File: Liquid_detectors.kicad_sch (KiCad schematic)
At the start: 1 part, among them U1 AD8021AR

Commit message: ahora modifique dos sch
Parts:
- added U2: AD8655, symbol Amplifier_Operational:AD8655
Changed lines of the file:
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@@
+		)
+	)
+	(symbol
+		(lib_id "Amplifier_Operational:AD8655")
+		(at 113.03 53.34 0)
+		(unit 1)
+		(exclude_from_sim no)
+		(in_bom yes)
+		(on_board yes)
+		(dnp no)
+		(fields_autoplaced yes)
+		(property "Reference" "U2"
+			(at 123.19 46.9198 0)
+			(effects
+				(font
+					(size 1.27 1.27)
+				)
+			)
+		)
+		(property "Value" "AD8655"
+			(at 123.19 49.4598 0)
+			(effects
+				(font
+					(size 1.27 1.27)
+				)
+			)
+		)
+		(property "Footprint" ""
+			(at 114.3 52.07 0)
+			(effects
+				(font
+					(size 1.27 1.27)
+				)
+				(hide yes)
+			)
+		)
+		(property "Datasheet" "https://www.analog.com/media/en/technical-documentation/data-sheets/ad8655_8656.pdf"
+			(at 116.84 49.53 0)
+			(effects
+				(font
+					(size 1.27 1.27)
+				)
+				(hide yes)
+			)
+		)
+		(property "Description" "Single Low Noise, Precision CMOS Amplifier"
+			(at 113.03 53.34 0)
+			(effects
+				(font
+					(size 1.27 1.27)
+				)
+				(hide yes)
+			)
+		)
+		(pin "3"
+		)
+		(pin "2"
+		)
+		(pin "7"
+		)
+		(pin "4"
+		)
+		(pin "8"
+		)
+		(pin "1"
+		)
+		(pin "5"
+		)
+		(pin "6"
+		)
+		(instances
+			(project ""
+				(path "/e23e72d0-3a4b-405e-bd06-0639cdab408e"
+					(reference "U2")
+					(unit 1)
+				)
+			)
 		)
 	)

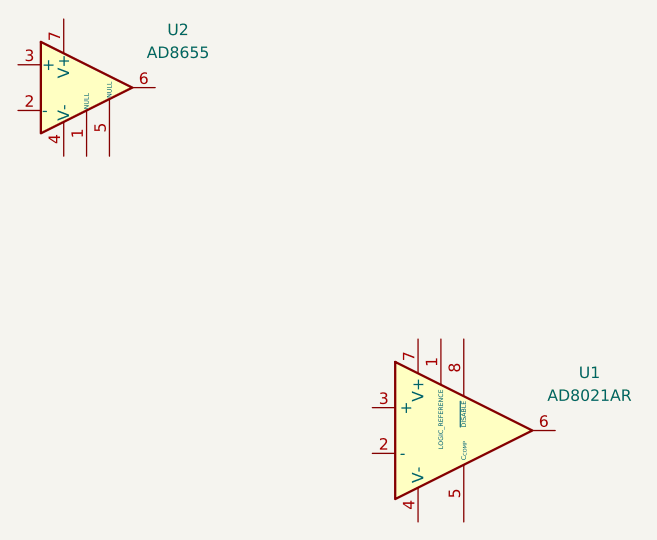
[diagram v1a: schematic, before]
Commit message: Revert "ahora modifique dos sch"
This reverts commit 6d1ee52be01612af9494df4d4ac0ee7ca94c663e.
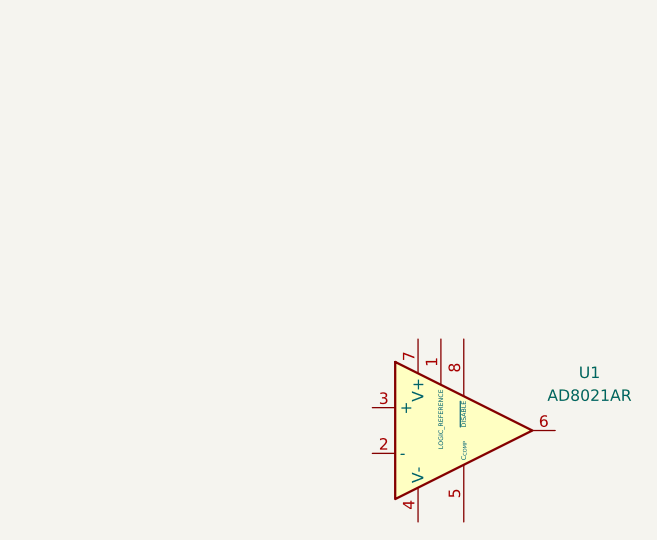
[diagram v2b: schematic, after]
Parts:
- removed U2: AD8655, symbol Amplifier_Operational:AD8655
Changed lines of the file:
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@@
-		)
-	)
-	(symbol
-		(lib_id "Amplifier_Operational:AD8655")
-		(at 113.03 53.34 0)
-		(unit 1)
-		(exclude_from_sim no)
-		(in_bom yes)
-		(on_board yes)
-		(dnp no)
-		(fields_autoplaced yes)
-		(property "Reference" "U2"
-			(at 123.19 46.9198 0)
-			(effects
-				(font
-					(size 1.27 1.27)
-				)
-			)
-		)
-		(property "Value" "AD8655"
-			(at 123.19 49.4598 0)
-			(effects
-				(font
-					(size 1.27 1.27)
-				)
-			)
-		)
-		(property "Footprint" ""
-			(at 114.3 52.07 0)
-			(effects
-				(font
-					(size 1.27 1.27)
-				)
-				(hide yes)
-			)
-		)
-		(property "Datasheet" "https://www.analog.com/media/en/technical-documentation/data-sheets/ad8655_8656.pdf"
-			(at 116.84 49.53 0)
-			(effects
-				(font
-					(size 1.27 1.27)
-				)
-				(hide yes)
-			)
-		)
-		(property "Description" "Single Low Noise, Precision CMOS Amplifier"
-			(at 113.03 53.34 0)
-			(effects
-				(font
-					(size 1.27 1.27)
-				)
-				(hide yes)
-			)
-		)
-		(pin "3"
-		)
-		(pin "2"
-		)
-		(pin "7"
-		)
-		(pin "4"
-		)
-		(pin "8"
-		)
-		(pin "1"
-		)
-		(pin "5"
-		)
-		(pin "6"
-		)
-		(instances
-			(project ""
-				(path "/e23e72d0-3a4b-405e-bd06-0639cdab408e"
-					(reference "U2")
-					(unit 1)
-				)
-			)
 		)
 	)
